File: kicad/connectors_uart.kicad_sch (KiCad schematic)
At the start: 4 parts, among them J3 USB_C_Receptacle_USB2.0_16P, U2 USBLC6-2SC6

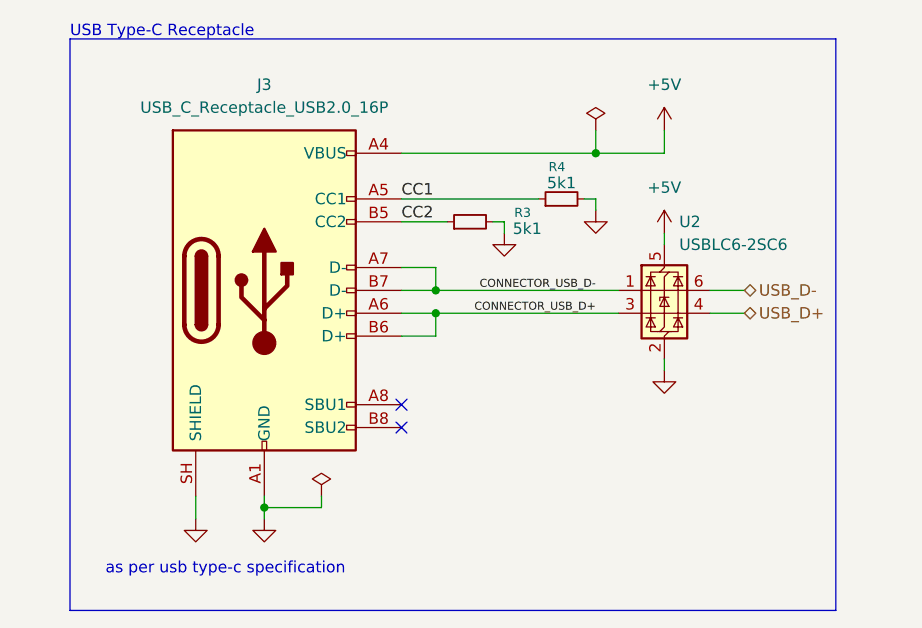
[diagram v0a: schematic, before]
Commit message: refactor(schematic): polish the schematic as much as possible - add new Basmala - fix netlist names almost EVERYWHERE, this is to help with net classes, and to help with building a good habit of naming nets properly - add a 100n capacitor to the SWD connector power pin - update many many other things EVERYWHERE
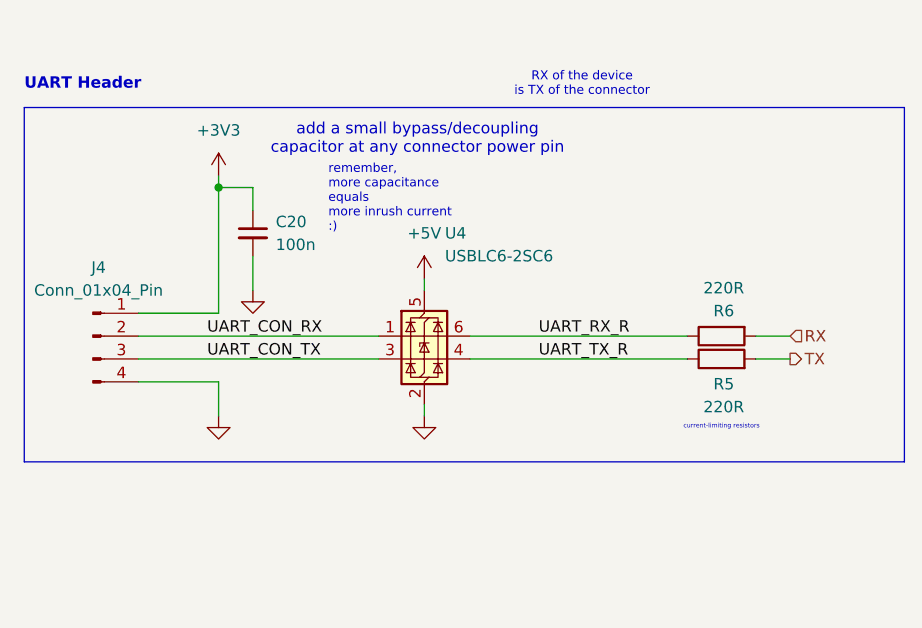
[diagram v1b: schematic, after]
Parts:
- removed J3: USB_C_Receptacle_USB2.0_16P, Connector_USB:USB_C_Receptacle_Amphenol_124019772112A, symbol Connector:USB_C_Receptacle_USB2.0_16P
- removed R3, R4: 5k1, symbol Device:R_Small
- removed U2: USBLC6-2SC6, Package_TO_SOT_SMD:SOT-23-6, symbol Power_Protection:USBLC6-2SC6
- added C20: 100n, symbol Device:C_Small
- added J4: Conn_01x04_Pin, symbol Connector:Conn_01x04_Pin
- added R5, R6: 220R, symbol Device:R
- added U4: USBLC6-2SC6, Package_TO_SOT_SMD:SOT-23-6, symbol Power_Protection:USBLC6-2SC6
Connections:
- net +5V: now also U4.5 (VBUS)
- net GND: now also C20.2, J4.4 (Pin_4), U4.2 (GND)
- new net +3V3: C20.1, J4.1 (Pin_1)
- new net RX: R6.2
- new net TX: R5.2
- new net UART_CON_RX: J4.2 (Pin_2), U4.1 (I/O1)
- new net UART_CON_TX: J4.3 (Pin_3), U4.3 (I/O2)
- new net UART_RX_R: R6.1, U4.6 (I/O1)
- new net UART_TX_R: R5.1, U4.4 (I/O2)
- no-connect marks 2 -> 0
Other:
- note added: "RX of the device is TX of the connector"
- note added: "UART Header"
- note added: "add a small bypass/decoupling capacitor at any connector power pin"
- note added: "current-limiting resistors"
- note added: "remember, more capacitance equals more inrush current :)"
- note removed: "USB Type-C Receptacle"
- note removed: "as per usb type-c specification"
